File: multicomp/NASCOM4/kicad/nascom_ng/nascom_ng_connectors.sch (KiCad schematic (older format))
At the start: 18 parts, among them J10 Conn_01x03_Male, J5 DB15_Female_HighDensity, J6 DB15_Female_HighDensity, J8 Conn_01x06, J9 Mini-DIN_6pins_ver2, U10 74HCT244

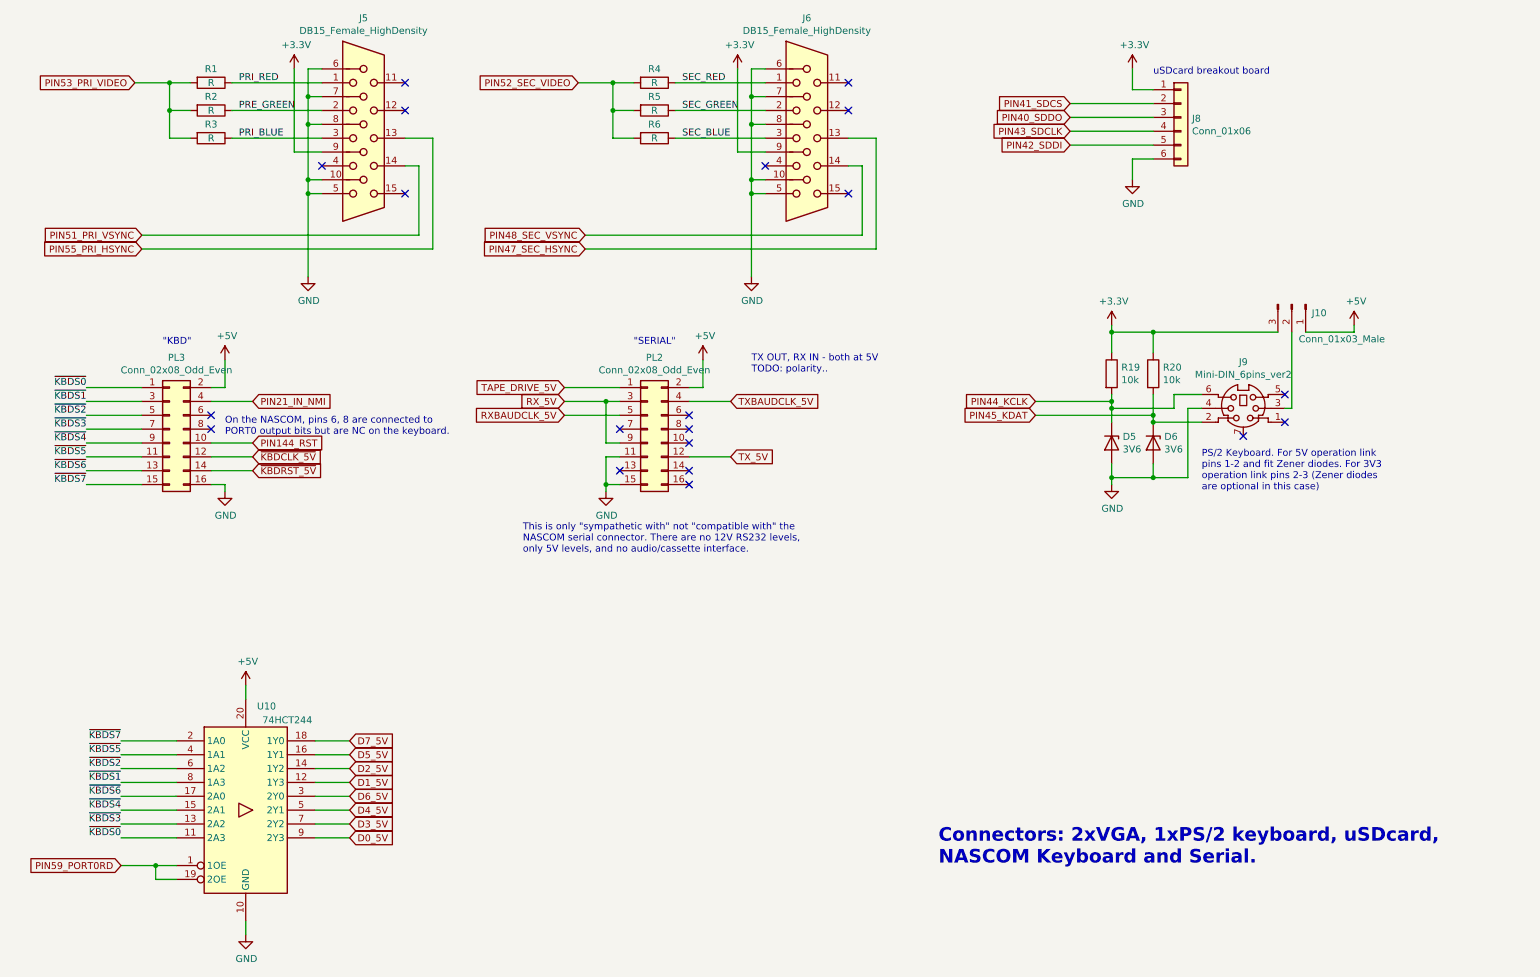
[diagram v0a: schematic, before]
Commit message: All nets routed, ref designators resequenced, nearly finished!
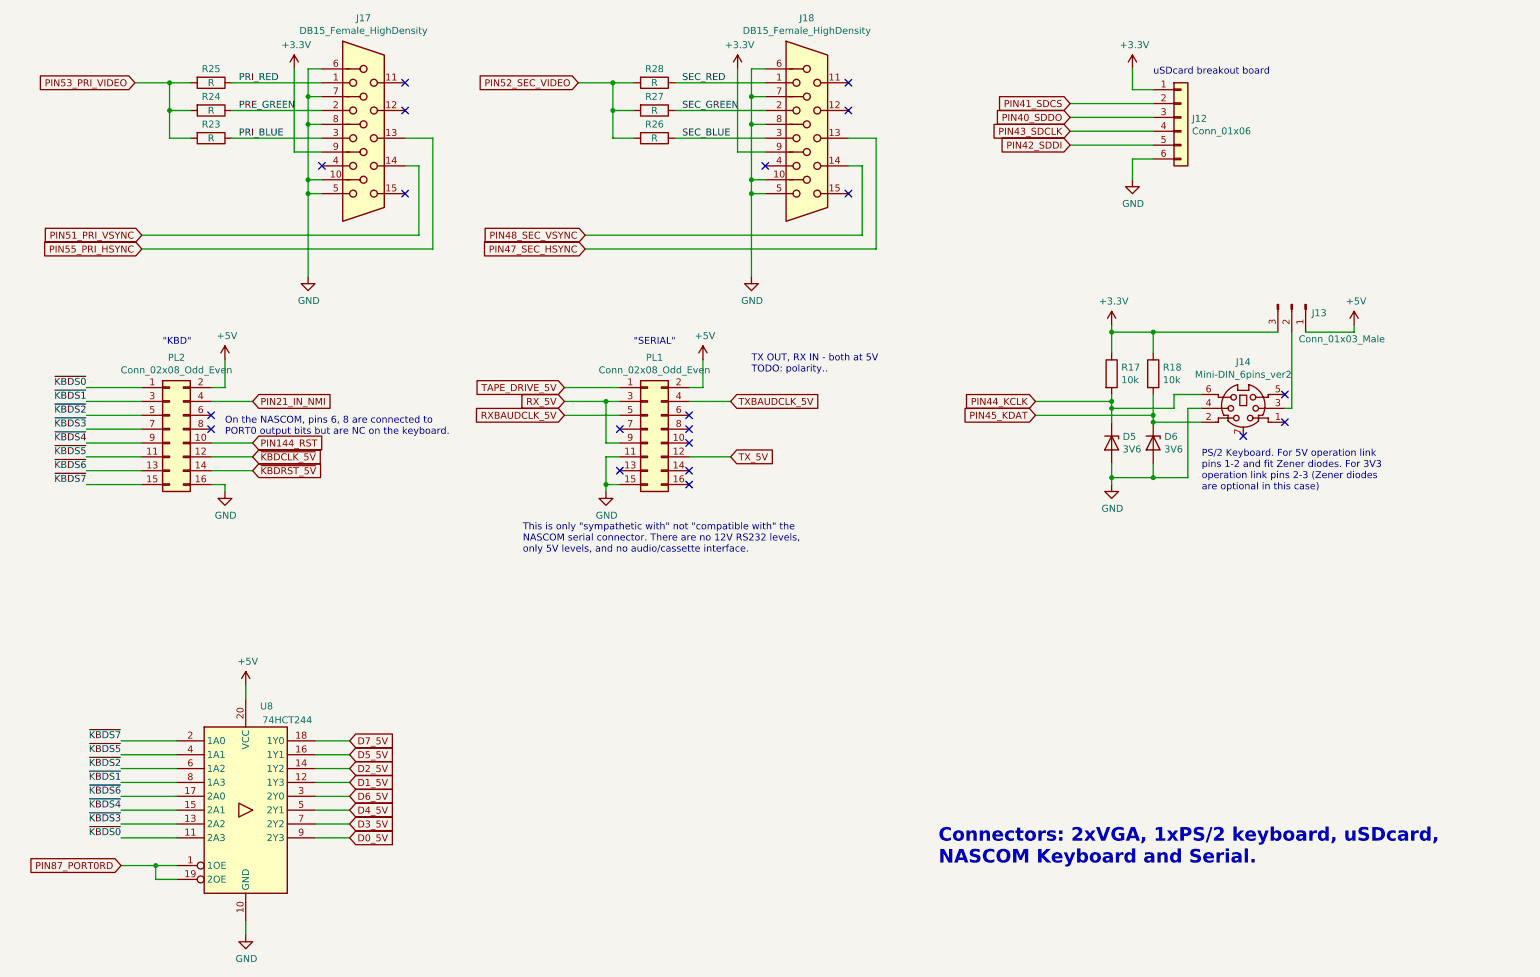
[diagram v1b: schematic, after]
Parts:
- renumbered J8 to J12, J10 to J13, J9 to J14, J5 to J17, J6 to J18, PL2 to PL1, PL3 to PL2, R19 to R17, R20 to R18, R3 to R23, R2 to R24, R1 to R25, R6 to R26, R5 to R27, R4 to R28, U10 to U8
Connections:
- net PIN59_PORT0RD renamed PIN87_PORT0RD
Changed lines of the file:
@@
 $EndDescr
 $Comp
-L Connector:DB15_Female_HighDensity J5
+L Connector:DB15_Female_HighDensity J17
 U 1 1 5FD8C4EA
 P 2950 1750
-F 0 "J5" H 2950 2617 50  0000 C CNN
+F 0 "J17" H 2950 2617 50  0000 C CNN
 F 1 "DB15_Female_HighDensity" H 2950 2526 50  0000 C CNN
 F 2 "Connector_Dsub:DSUB-15-HD_Female_Horizontal_P2.29x1.98mm_EdgePinOffset3.03mm_Housed_MountingHolesOffset4.94mm" H 2000 2150 50  0001 C CNN
@@
 $EndComp
 $Comp
-L Device:R R1
+L Device:R R25
 U 1 1 5FD8D7B7
 P 1850 1350
-F 0 "R1" V 1750 1350 50  0000 C CNN
+F 0 "R25" V 1750 1350 50  0000 C CNN
 F 1 "R" V 1850 1350 50  0000 C CNN
 F 2 "Resistor_THT:R_Axial_DIN0204_L3.6mm_D1.6mm_P7.62mm_Horizontal" V 1780 1350 50  0001 C CNN
@@
 $EndComp
 $Comp
-L Device:R R2
+L Device:R R24
 U 1 1 5FD8DEB7
 P 1850 1550
-F 0 "R2" V 1750 1550 50  0000 C CNN
+F 0 "R24" V 1750 1550 50  0000 C CNN
 F 1 "R" V 1850 1550 50  0000 C CNN
 F 2 "Resistor_THT:R_Axial_DIN0204_L3.6mm_D1.6mm_P7.62mm_Horizontal" V 1780 1550 50  0001 C CNN
@@
 $EndComp
 $Comp
-L Device:R R3
+L Device:R R23
 U 1 1 5FD8E0C3
 P 1850 1750
-F 0 "R3" V 1750 1750 50  0000 C CNN
+F 0 "R23" V 1750 1750 50  0000 C CNN
 F 1 "R" V 1850 1750 50  0000 C CNN
 F 2 "Resistor_THT:R_Axial_DIN0204_L3.6mm_D1.6mm_P7.62mm_Horizontal" V 1780 1750 50  0001 C CNN
@@
 $EndComp
 $Comp
-L Connector:DB15_Female_HighDensity J6
+L Connector:DB15_Female_HighDensity J18
 U 1 1 5FD94BC5
 P 6150 1750
-F 0 "J6" H 6150 2617 50  0000 C CNN
+F 0 "J18" H 6150 2617 50  0000 C CNN
 F 1 "DB15_Female_HighDensity" H 6150 2526 50  0000 C CNN
 F 2 "Connector_Dsub:DSUB-15-HD_Female_Horizontal_P2.29x1.98mm_EdgePinOffset3.03mm_Housed_MountingHolesOffset4.94mm" H 5200 2150 50  0001 C CNN
@@
 $EndComp
 $Comp
-L Device:R R4
+L Device:R R28
 U 1 1 5FD94BCF
 P 5050 1350
-F 0 "R4" V 4950 1350 50  0000 C CNN
+F 0 "R28" V 4950 1350 50  0000 C CNN
 F 1 "R" V 5050 1350 50  0000 C CNN
 F 2 "Resistor_THT:R_Axial_DIN0204_L3.6mm_D1.6mm_P7.62mm_Horizontal" V 4980 1350 50  0001 C CNN
@@
 $EndComp
 $Comp
-L Device:R R5
+L Device:R R27
 U 1 1 5FD94BD9
 P 5050 1550
-F 0 "R5" V 4950 1550 50  0000 C CNN
+F 0 "R27" V 4950 1550 50  0000 C CNN
 F 1 "R" V 5050 1550 50  0000 C CNN
 F 2 "Resistor_THT:R_Axial_DIN0204_L3.6mm_D1.6mm_P7.62mm_Horizontal" V 4980 1550 50  0001 C CNN
@@
 $EndComp
 $Comp
-L Device:R R6
+L Device:R R26
 U 1 1 5FD94BE3
 P 5050 1750
-F 0 "R6" V 4950 1750 50  0000 C CNN
+F 0 "R26" V 4950 1750 50  0000 C CNN
 F 1 "R" V 5050 1750 50  0000 C CNN
 F 2 "Resistor_THT:R_Axial_DIN0204_L3.6mm_D1.6mm_P7.62mm_Horizontal" V 4980 1750 50  0001 C CNN
@@
 	8650 1900 8500 1900
 $Comp
-L Device:R R19
+L Device:R R17
 U 1 1 60792D3D
 P 8350 3450
-F 0 "R19" H 8420 3496 50  0000 L CNN
+F 0 "R17" H 8420 3496 50  0000 L CNN
 F 1 "10k" H 8420 3405 50  0000 L CNN
 F 2 "Resistor_THT:R_Axial_DIN0204_L3.6mm_D1.6mm_P7.62mm_Horizontal" V 8280 3450 50  0001 C CNN
@@
 $EndComp
 $Comp
-L Device:R R20
+L Device:R R18
 U 1 1 607938E7
 P 8650 3450
-F 0 "R20" H 8720 3496 50  0000 L CNN
+F 0 "R18" H 8720 3496 50  0000 L CNN
 F 1 "10k" H 8720 3405 50  0000 L CNN
 F 2 "Resistor_THT:R_Axial_DIN0204_L3.6mm_D1.6mm_P7.62mm_Horizontal" V 8580 3450 50  0001 C CNN
@@
 	8350 3150 8350 3300
 $Comp
-L Connector:Conn_01x03_Male J10
+L Connector:Conn_01x03_Male J13
 U 1 1 607AD886
 P 9650 2950
-F 0 "J10" V 9712 3094 50  0000 L CNN
+F 0 "J13" V 9712 3094 50  0000 L CNN
 F 1 "Conn_01x03_Male" V 9900 3000 50  0000 L CNN
 F 2 "Connector_PinHeader_2.54mm:PinHeader_1x03_P2.54mm_Vertical" H 9650 2950 50  0001 C CNN
@@
 P 1550 3850
 AR Path="/5FC877BB/60D96959" Ref="PL?"  Part="1"
-AR Path="/5FC85C78/60D96959" Ref="PL3"  Part="1"
-F 0 "PL3" H 1600 4367 50  0000 C CNN
+AR Path="/5FC85C78/60D96959" Ref="PL2"  Part="1"
+F 0 "PL2" H 1600 4367 50  0000 C CNN
 F 1 "Conn_02x08_Odd_Even" H 1600 4276 50  0000 C CNN
 F 2 "Connector_IDC:IDC-Header_2x08_P2.54mm_Vertical" H 1550 3850 50  0001 C CNN
@@
 P 5000 3850
 AR Path="/5FC877BB/60D9695F" Ref="J?"  Part="1"
-AR Path="/5FC85C78/60D9695F" Ref="PL2"  Part="1"
-F 0 "PL2" H 5050 4367 50  0000 C CNN
+AR Path="/5FC85C78/60D9695F" Ref="PL1"  Part="1"
+F 0 "PL1" H 5050 4367 50  0000 C CNN
 F 1 "Conn_02x08_Odd_Even" H 5050 4276 50  0000 C CNN
 F 2 "Connector_IDC:IDC-Header_2x08_P2.54mm_Vertical" H 5000 3850 50  0001 C CNN
@@
 AR Path="/5FC86EA5/60D96965" Ref="U?"  Part="1"
 AR Path="/5FC877BB/60D96965" Ref="U?"  Part="1"
-AR Path="/5FC85C78/60D96965" Ref="U10"  Part="1"
-F 0 "U10" H 2250 7350 50  0000 C CNN
+AR Path="/5FC85C78/60D96965" Ref="U8"  Part="1"
+F 0 "U8" H 2250 7350 50  0000 C CNN
 F 1 "74HCT244" H 2400 7250 50  0000 C CNN
 F 2 "Package_DIP:DIP-20_W7.62mm" H 2100 6600 50  0001 C CNN
@@
 Connection ~ 1450 7000
 Text GLabel 1200 7000 0    50   Input ~ 0
-PIN59_PORT0RD
+PIN87_PORT0RD
 $Comp
 L power:GND #PWR?
@@
 NoConn ~ 5300 4250
 $Comp
-L Connector_Generic:Conn_01x06 J8
+L Connector_Generic:Conn_01x06 J12
 U 1 1 602BDB1D
 P 8850 1600
-F 0 "J8" H 8930 1592 50  0000 L CNN
+F 0 "J12" H 8930 1592 50  0000 L CNN
 F 1 "Conn_01x06" H 8930 1501 50  0000 L CNN
 F 2 "mylib:uSDcard_breakout_1x06_P2.54mm" H 8850 1600 50  0001 C CNN
@@
 	2600 6500 2850 6500
 $Comp
-L myLib:Mini-DIN_6pins_ver2 J9
+L myLib:Mini-DIN_6pins_ver2 J14
 U 1 1 604A5287
 P 9300 3700
-F 0 "J9" H 9300 4035 50  0000 C CNN
+F 0 "J14" H 9300 4035 50  0000 C CNN
 F 1 "Mini-DIN_6pins_ver2" H 9300 3944 50  0000 C CNN
 F 2 "mylib:Connector_Mini-DIN_Female_6Pin_2rows" H 9300 3720 50  0001 C CNN

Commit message: Files for REV A release to PCB manufacture
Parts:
- renumbered J13 to J12, J14 to J13, J12 to J19, PL1 to PL2, PL2 to PL3
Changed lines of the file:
@@
 	8350 3150 8350 3300
 $Comp
-L Connector:Conn_01x03_Male J13
+L Connector:Conn_01x03_Male J12
 U 1 1 607AD886
 P 9650 2950
-F 0 "J13" V 9712 3094 50  0000 L CNN
+F 0 "J12" V 9712 3094 50  0000 L CNN
 F 1 "Conn_01x03_Male" V 9900 3000 50  0000 L CNN
 F 2 "Connector_PinHeader_2.54mm:PinHeader_1x03_P2.54mm_Vertical" H 9650 2950 50  0001 C CNN
@@
 P 1550 3850
 AR Path="/5FC877BB/60D96959" Ref="PL?"  Part="1"
-AR Path="/5FC85C78/60D96959" Ref="PL2"  Part="1"
-F 0 "PL2" H 1600 4367 50  0000 C CNN
+AR Path="/5FC85C78/60D96959" Ref="PL3"  Part="1"
+F 0 "PL3" H 1600 4367 50  0000 C CNN
 F 1 "Conn_02x08_Odd_Even" H 1600 4276 50  0000 C CNN
 F 2 "Connector_IDC:IDC-Header_2x08_P2.54mm_Vertical" H 1550 3850 50  0001 C CNN
@@
 P 5000 3850
 AR Path="/5FC877BB/60D9695F" Ref="J?"  Part="1"
-AR Path="/5FC85C78/60D9695F" Ref="PL1"  Part="1"
-F 0 "PL1" H 5050 4367 50  0000 C CNN
+AR Path="/5FC85C78/60D9695F" Ref="PL2"  Part="1"
+F 0 "PL2" H 5050 4367 50  0000 C CNN
 F 1 "Conn_02x08_Odd_Even" H 5050 4276 50  0000 C CNN
 F 2 "Connector_IDC:IDC-Header_2x08_P2.54mm_Vertical" H 5000 3850 50  0001 C CNN
@@
 NoConn ~ 5300 4250
 $Comp
-L Connector_Generic:Conn_01x06 J12
+L Connector_Generic:Conn_01x06 J19
 U 1 1 602BDB1D
 P 8850 1600
-F 0 "J12" H 8930 1592 50  0000 L CNN
+F 0 "J19" H 8930 1592 50  0000 L CNN
 F 1 "Conn_01x06" H 8930 1501 50  0000 L CNN
 F 2 "mylib:uSDcard_breakout_1x06_P2.54mm" H 8850 1600 50  0001 C CNN
@@
 	2600 6500 2850 6500
 $Comp
-L myLib:Mini-DIN_6pins_ver2 J14
+L myLib:Mini-DIN_6pins_ver2 J13
 U 1 1 604A5287
 P 9300 3700
-F 0 "J14" H 9300 4035 50  0000 C CNN
+F 0 "J13" H 9300 4035 50  0000 C CNN
 F 1 "Mini-DIN_6pins_ver2" H 9300 3944 50  0000 C CNN
 F 2 "mylib:Connector_Mini-DIN_Female_6Pin_2rows" H 9300 3720 50  0001 C CNN

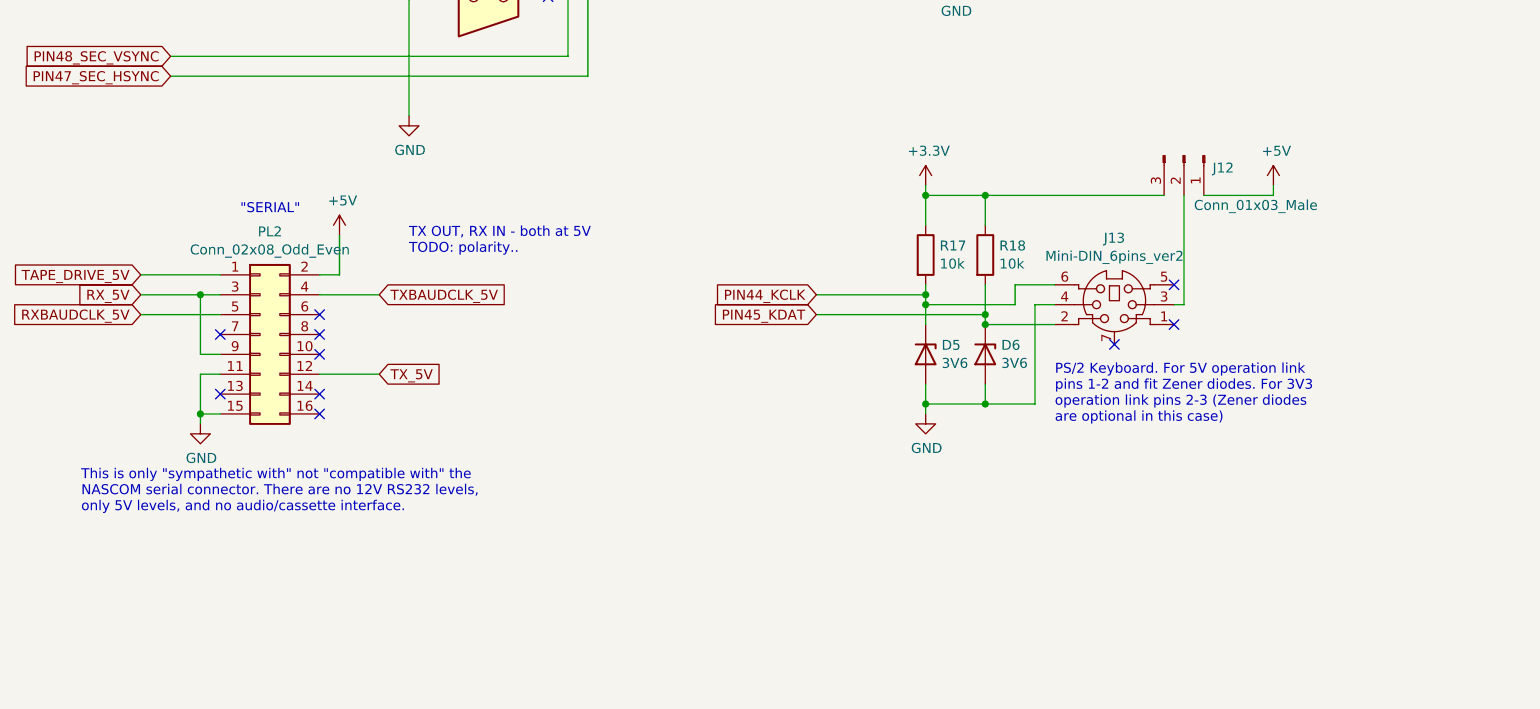
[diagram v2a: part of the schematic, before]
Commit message: Add REVB data-base: schematics, pcb and manufacturing files
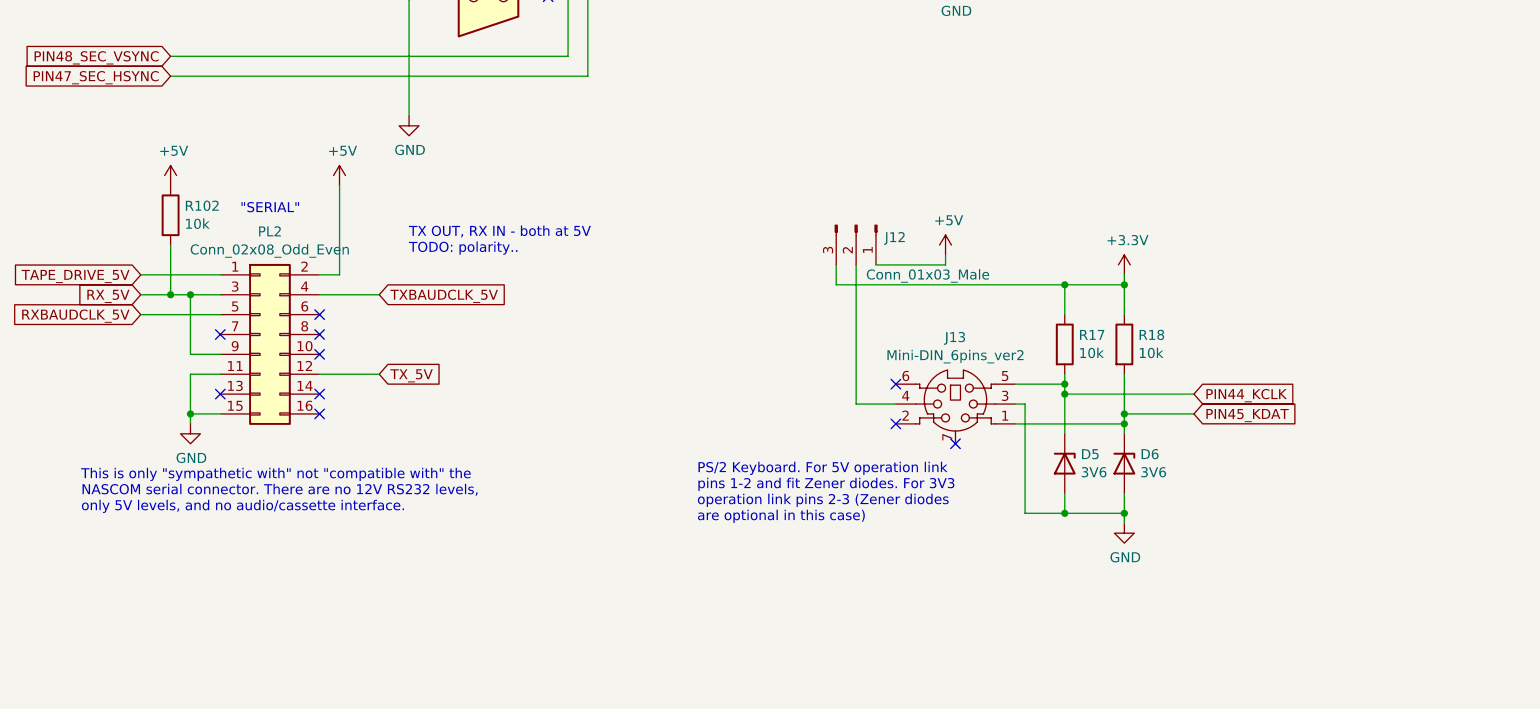
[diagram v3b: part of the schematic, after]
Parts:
- added R102: 10k, Resistor_THT:R_Axial_DIN0204_L3.6mm_D1.6mm_P7.62mm_Horizontal, symbol Device:R
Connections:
- net +5V: now also R102.1
- net GND: now also J13.3; no longer J13.4
- net PIN44_KCLK: now also J13.5; no longer J13.6
- net PIN45_KDAT: now also J13.1; no longer J13.2
- net RX_5V: now also R102.2
- net at J12.2 (Pin_2): now also J13.4; no longer J13.3
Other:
- moved on the sheet: D5, D6, J12, J13, R17, R18
